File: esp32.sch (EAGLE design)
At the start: 2 parts, among them IC1 PEC11R-4230K-S0024, U1 ESP32-WROOM-32D

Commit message: Stora dela av schematic är klart. Saknar fortfarande vissa viktiga delar, men då måste jag passera admittansen först.
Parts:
- added 5V_REG_CON, WS2812B_CON: (no value), SparkFun-Connectors:CONN_03
- added BAT_CON, SPEAKER_OUT: (no value), SparkFun-Connectors:CONN_02
- added C1, C2, C3, C4, C5, C6: (no value), rcl:C-EUC0603
- added C7, C8: 10uF, rcl:C-EUC0603
- added C9: 270uF, rcl:C-EUC0603
- added DS1: (no value), Test:NHD-0216XZ-FSW-GBWNHD0216XZFSWGBW_DUPONTCONNECTOR
- added IC2: AD8532ARZ, Test:AD8532ARZ
- added JP1, JP2: (no value), pinhead:PINHD-1X2
- added R1, R10, R12, R14, R2, R3, R4, R5, R6, R8: 10k, rcl:R-EU_R0603
- added R11, R13, R22, R7, R9: 100, rcl:R-EU_R0603
- added R15, R16: (no value), rcl:R-EU_R0603
- added R17, R18, R21: 50k, rcl:R-EU_R0603
- added R19: 100k, rcl:R-EU_R0603
- added R20: 16, rcl:R-EU_R0603
- added T1, T2: BST82-1, Test:BST82-1
- added U$1, U$2, U$3: PUSH_BUTTON, Test:PUSH_BUTTON
- added U$4: A1SHB, Test:A1SHB
- added U$5: ESP32_CON_JTAG, Test:ESP32_CON_JTAG
- added U$6: ESP32_CON_PROG, Test:ESP32_CON_PROG
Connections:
- new net +3V3: IC1.COM, R3.1, R4.1, U$1.1, U$1.2, U$2.1, U$2.2, U$3.1, U$3.2
- new net +5V: 5V_REG_CON.2, WS2812B_CON.1
- new net AUDIO_FROM_ESP32: C8.1
- new net BAT_MONITOR_ANALOG: R15.2, R16.1
- new net BAT_MONITOR_ENABLE: R13.2
- new net BTN_1: R7.1
- new net BTN_2: R9.1
- new net BTN_3: R11.1
- new net ENABLE_5V: R22.2
- new net ESP_EN: U$6.EN
- new net ESP_IO_0: U$6.IO_0
- new net ESP_RX: U$6.ESP_RX
- new net ESP_TX: U$6.ESP_TX
- new net GND: BAT_CON.2, C1.2, C2.2, C3.2, C4.2, C5.2, C6.2, IC1.C, IC2.V-, R10.1, R12.1, R16.2, R19.1, R21.2, R6.1, R8.1, SPEAKER_OUT.2, T1.S, T2.S, U$5.GND, U$6.GND, WS2812B_CON.3
- new net N$1: IC1.A, R1.2, R3.2
- new net N$10: C7.1, R17.1, R18.2
- new net N$11: R22.1, T2.G
- new net N$12: IC2.-INA, IC2.OUTA, R20.2
- new net N$13: R13.1, T1.G
- new net N$14: C9.1, R20.1
- new net N$15: 5V_REG_CON.3, T2.D
- new net N$2: IC1.B, R2.1, R4.2
- new net N$22: JP2.2, U$6.VDD
- new net N$23: JP2.1
- new net N$24: JP1.1, U$5.VDD
- new net N$25: JP1.2
- new net N$3: C4.1, R7.2, R8.2, U$1.3, U$1.4
- new net N$4: C8.2, IC2.+INA, R18.1, R19.2
- new net N$5: R15.1, U$4.D
- new net N$6: C5.1, R10.2, R9.2, U$2.3, U$2.4
- new net N$7: R14.2, T1.D, U$4.G
- new net N$8: C6.1, R11.2, R12.2, U$3.3, U$3.4
- new net N$9: C3.1, IC1.NO, R5.2, R6.2
- new net ROT_ENC_A: C1.1, R1.1
- new net ROT_ENC_B: C2.1, R2.2
- new net ROT_ENC_BTN: R5.1
- new net SPEAKER_OUT: C9.2, R21.1, SPEAKER_OUT.1
- new net TCK: U$5.TCK
- new net TDI: U$5.TDI
- new net TDO: U$5.TDO
- new net TMS: U$5.TMS
- new net VCC: 5V_REG_CON.1, BAT_CON.1, IC2.V+, R14.1, R17.2, U$4.S
- new net WS2812B_DATA: WS2812B_CON.2
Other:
- note added: "3.3V regulator här sen tack"

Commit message: Lite grovt upplägg av vissa komponenter på kortet.
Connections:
- net +3V3: now also U1.3V3
- net AUDIO_FROM_ESP32: now also U1.IO26
- net ESP_EN: now also U1.EN
- net ESP_IO_0: now also U1.IO25
- net ESP_RX: now also U1.RXD0
- net ESP_TX: now also U1.TXD0
- net GND: now also C7.2, U1.GND
- net TCK: now also U1.IO13
- net TDI: now also U1.IO12
- net TDO: now also U1.IO15
- net TMS: now also U1.IO14
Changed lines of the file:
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@@
 <part name="GND17" library="supply1" library_urn="urn:adsk.eagle:library:371" deviceset="GND" device=""/>
 <part name="GND18" library="supply1" library_urn="urn:adsk.eagle:library:371" deviceset="GND" device=""/>
+<part name="GND19" library="supply1" library_urn="urn:adsk.eagle:library:371" deviceset="GND" device=""/>
+<part name="GND20" library="supply1" library_urn="urn:adsk.eagle:library:371" deviceset="GND" device=""/>
+<part name="+3V6" library="supply1" library_urn="urn:adsk.eagle:library:371" deviceset="+3V3" device=""/>
 </parts>
 <sheets>
@@
 <attribute name="VALUE" x="121.92" y="119.38" size="1.778" layer="96"/>
 </instance>
+<instance part="GND20" gate="1" x="83.82" y="81.28" smashed="yes">
+<attribute name="VALUE" x="81.28" y="78.74" size="1.778" layer="96"/>
+</instance>
+<instance part="+3V6" gate="G$1" x="83.82" y="160.02" smashed="yes">
+<attribute name="VALUE" x="81.28" y="154.94" size="1.778" layer="96" rot="R90"/>
+</instance>
 </instances>
 <busses>
@@
 <wire x1="167.64" y1="93.98" x2="167.64" y2="76.2" width="0.1524" layer="91"/>
 </segment>
+<segment>
+<pinref part="U1" gate="G$1" pin="GND"/>
+<wire x1="81.28" y1="91.44" x2="83.82" y2="91.44" width="0.1524" layer="91"/>
+<wire x1="83.82" y1="91.44" x2="83.82" y2="83.82" width="0.1524" layer="91"/>
+<pinref part="GND20" gate="1" pin="GND"/>
+</segment>
 </net>
 <net name="+5V" class="0">
@@
 <label x="165.1" y="142.24" size="1.778" layer="95" xref="yes"/>
 </segment>
+<segment>
+<pinref part="U1" gate="G$1" pin="IO14"/>
+<wire x1="81.28" y1="129.54" x2="93.98" y2="129.54" width="0.1524" layer="91"/>
+<label x="93.98" y="129.54" size="1.778" layer="95" xref="yes"/>
+</segment>
 </net>
 <net name="TCK" class="0">
@@
 <label x="165.1" y="137.16" size="1.778" layer="95" xref="yes"/>
 </segment>
+<segment>
+<pinref part="U1" gate="G$1" pin="IO13"/>
+<wire x1="81.28" y1="132.08" x2="86.36" y2="132.08" width="0.1524" layer="91"/>
+<label x="86.36" y="132.08" size="1.778" layer="95" xref="yes"/>
+</segment>
 </net>
 <net name="TDO" class="0">
@@
 <wire x1="160.02" y1="132.08" x2="165.1" y2="132.08" width="0.1524" layer="91"/>
 <label x="165.1" y="132.08" size="1.778" layer="95" xref="yes"/>
+</segment>
+<segment>
+<pinref part="U1" gate="G$1" pin="IO15"/>
+<wire x1="81.28" y1="127" x2="86.36" y2="127" width="0.1524" layer="91"/>
+<label x="86.36" y="127" size="1.778" layer="95" xref="yes"/>
 </segment>
 </net>
@@
 <label x="165.1" y="127" size="1.778" layer="95" xref="yes"/>
 </segment>
+<segment>
+<pinref part="U1" gate="G$1" pin="IO12"/>
+<wire x1="81.28" y1="134.62" x2="93.98" y2="134.62" width="0.1524" layer="91"/>
+<label x="93.98" y="134.62" size="1.778" layer="95" xref="yes"/>
+</segment>
 </net>
 <net name="N$22" class="0">
@@
 <wire x1="132.08" y1="99.06" x2="132.08" y2="96.52" width="0.1524" layer="91"/>
 </segment>
+<segment>
+<pinref part="U1" gate="G$1" pin="EN"/>
+<wire x1="40.64" y1="144.78" x2="38.1" y2="144.78" width="0.1524" layer="91"/>
+<label x="38.1" y="144.78" size="1.778" layer="95" rot="R180" xref="yes"/>
+</segment>
 </net>
 <net name="ESP_TX" class="0">
@@
 <wire x1="134.62" y1="93.98" x2="132.08" y2="93.98" width="0.1524" layer="91"/>
 <label x="132.08" y="93.98" size="1.778" layer="95" rot="R180" xref="yes"/>
+</segment>
+<segment>
+<pinref part="U1" gate="G$1" pin="TXD0"/>
+<wire x1="40.64" y1="121.92" x2="38.1" y2="121.92" width="0.1524" layer="91"/>
+<label x="38.1" y="124.46" size="1.778" layer="95" rot="R180" xref="yes"/>
+<wire x1="38.1" y1="121.92" x2="38.1" y2="124.46" width="0.1524" layer="91"/>
 </segment>
 </net>
@@
 <wire x1="132.08" y1="91.44" x2="132.08" y2="88.9" width="0.1524" layer="91"/>
 </segment>
+<segment>
+<pinref part="U1" gate="G$1" pin="RXD0"/>
+<wire x1="40.64" y1="119.38" x2="38.1" y2="119.38" width="0.1524" layer="91"/>
+<label x="38.1" y="116.84" size="1.778" layer="95" rot="R180" xref="yes"/>
+<wire x1="38.1" y1="119.38" x2="38.1" y2="116.84" width="0.1524" layer="91"/>
+</segment>
 </net>
 <net name="ESP_IO_0" class="0">
@@
 <wire x1="165.1" y1="91.44" x2="170.18" y2="91.44" width="0.1524" layer="91"/>
 <label x="170.18" y="91.44" size="1.778" layer="95" xref="yes"/>
+</segment>
+<segment>
+<pinref part="U1" gate="G$1" pin="IO25"/>
+<wire x1="81.28" y1="106.68" x2="88.9" y2="106.68" width="0.1524" layer="91"/>
+<label x="88.9" y="106.68" size="1.778" layer="95" xref="yes"/>
+</segment>
+</net>
+<net name="+3V3" class="0">
+<segment>
+<pinref part="U1" gate="G$1" pin="3V3"/>
+<wire x1="81.28" y1="149.86" x2="83.82" y2="149.86" width="0.1524" layer="91"/>
+<wire x1="83.82" y1="149.86" x2="83.82" y2="157.48" width="0.1524" layer="91"/>
+<pinref part="+3V6" gate="G$1" pin="+3V3"/>
+</segment>
+</net>
+<net name="AUDIO_FROM_ESP32" class="0">
+<segment>
+<pinref part="U1" gate="G$1" pin="IO26"/>
+<wire x1="81.28" y1="104.14" x2="83.82" y2="104.14" width="0.1524" layer="91"/>
+<label x="83.82" y="104.14" size="1.778" layer="95" xref="yes"/>
 </segment>
 </net>
@@
 </instance>
 <instance part="R8" gate="G$1" x="185.42" y="144.78" smashed="yes" rot="R90">
-<attribute name="NAME" x="183.9214" y="140.97" size="1.778" layer="95" rot="R90"/>
-<attribute name="VALUE" x="188.722" y="140.97" size="1.778" layer="96" rot="R90"/>
+<attribute name="NAME" x="178.8414" y="140.97" size="1.778" layer="95" rot="R90"/>
+<attribute name="VALUE" x="183.642" y="140.97" size="1.778" layer="96" rot="R90"/>
 </instance>
 <instance part="C4" gate="G$1" x="193.04" y="147.32" smashed="yes">
@@
 <attribute name="VALUE" x="137.16" y="48.26" size="1.778" layer="96"/>
 </instance>
+<instance part="GND19" gate="1" x="66.04" y="45.72" smashed="yes">
+<attribute name="VALUE" x="63.5" y="43.18" size="1.778" layer="96"/>
+</instance>
 </instances>
 <busses>
@@
 <wire x1="139.7" y1="53.34" x2="139.7" y2="60.96" width="0.1524" layer="91"/>
 </segment>
-</net>
+<segment>
+<pinref part="GND19" gate="1" pin="GND"/>
+<pinref part="C7" gate="G$1" pin="2"/>
+<wire x1="66.04" y1="48.26" x2="66.04" y2="50.8" width="0.1524" layer="91"/>
+</segment>
+</net>

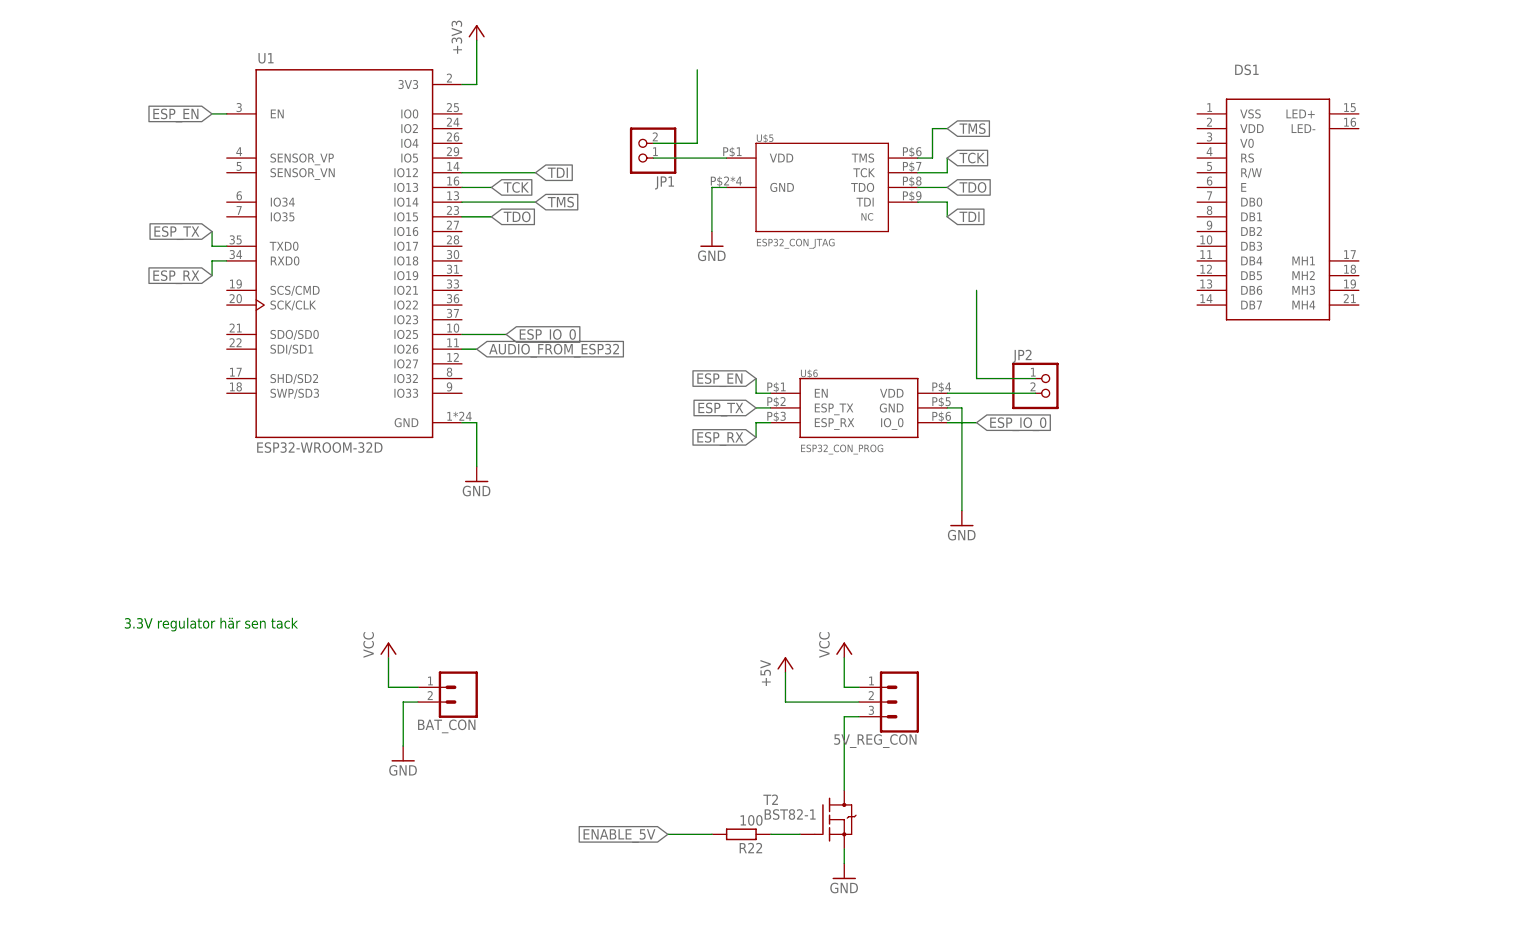
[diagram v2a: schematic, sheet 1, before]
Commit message: Bra upplägg på kortet men saknar fortfarande 3.3V regulator.
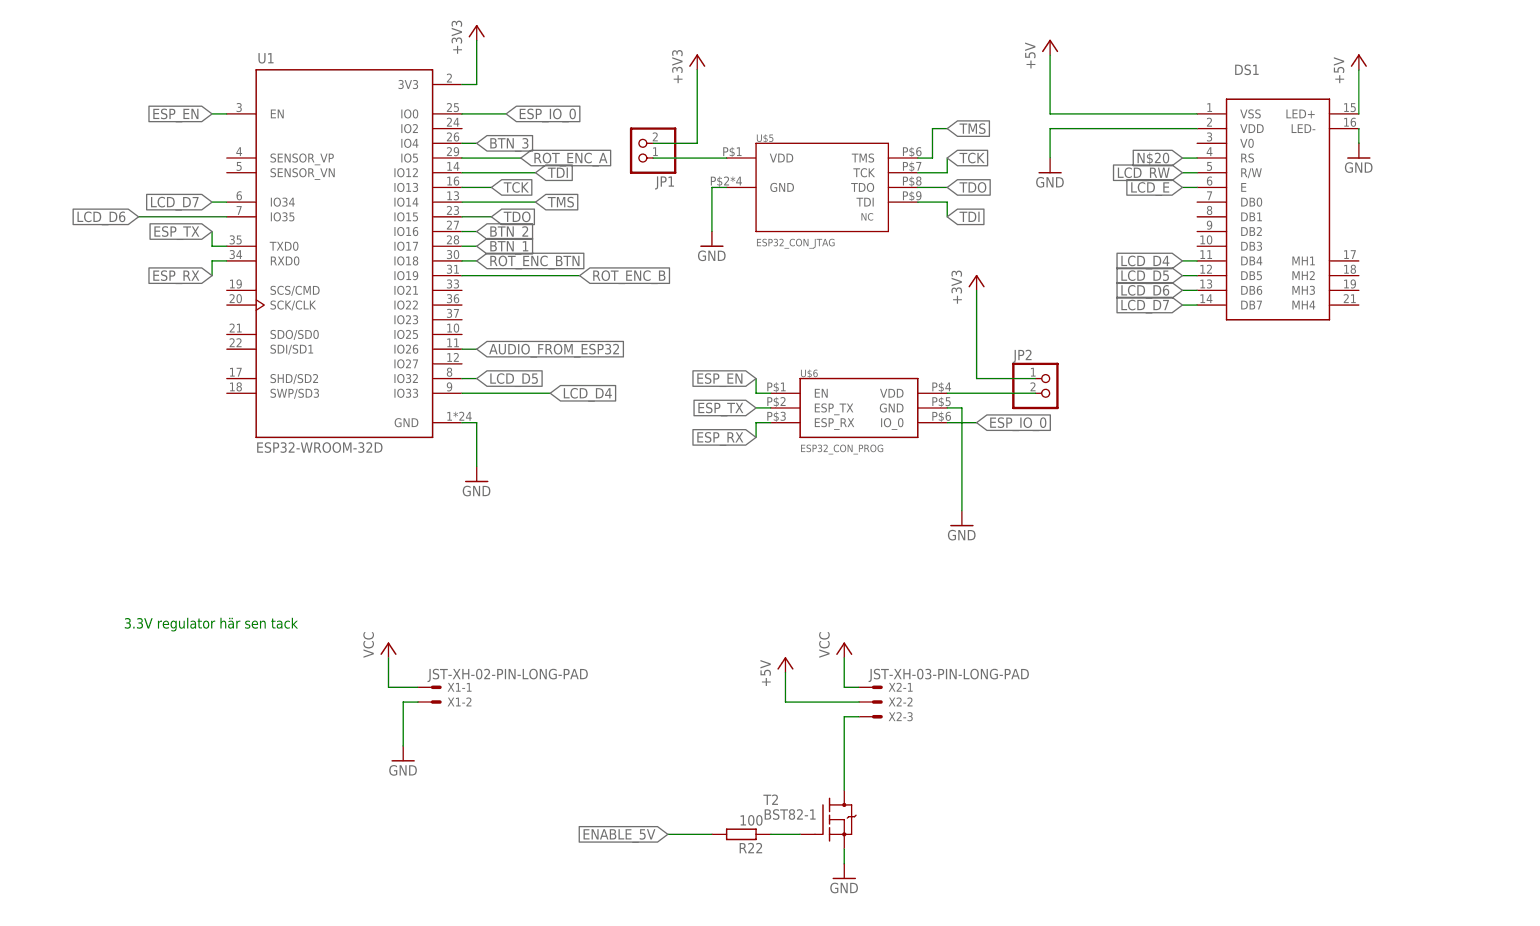
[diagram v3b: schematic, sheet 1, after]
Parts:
- removed 5V_REG_CON, WS2812B_CON: (no value), SparkFun-Connectors:CONN_03
- removed BAT_CON, SPEAKER_OUT: (no value), SparkFun-Connectors:CONN_02
- added X1, X4: JST-XH-02-PIN-LONG-PAD, Rembrandt Electronics - JST XH Connectors v1-0:JST-XH-02-PIN-LONG-PAD
- added X2, X3: JST-XH-03-PIN-LONG-PAD, Rembrandt Electronics - JST XH Connectors v1-0:JST-XH-03-PIN-LONG-PAD
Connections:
- removed net N$23: JP2.1
- removed net N$25: JP1.2
- new net LCD_D4: DS1.DB4, U1.IO33
- new net LCD_D5: DS1.DB5, U1.IO32
- new net LCD_D6: DS1.DB6, U1.IO35
- new net LCD_D7: DS1.DB7, U1.IO34
- new net LCD_E: DS1.E
- new net LCD_RW: DS1.R/W
- new net N$20: DS1.RS
- net +3V3: now also JP1.2, JP2.1
- net +5V: now also DS1.LED+, DS1.VSS, X2-2.S, X3-1.S; no longer 5V_REG_CON.2, WS2812B_CON.1
- net BTN_1: now also U1.IO17
- net BTN_2: now also U1.IO16
- net BTN_3: now also U1.IO4
- net ESP_IO_0: now also U1.IO0; no longer U1.IO25
- net GND: now also DS1.LED-, DS1.VDD, X1-2.S, X3-3.S, X4-2.S; no longer BAT_CON.2, SPEAKER_OUT.2, WS2812B_CON.3
- net N$15: now also X2-3.S; no longer 5V_REG_CON.3
- net ROT_ENC_A: now also U1.IO5
- net ROT_ENC_B: now also U1.IO19
- net ROT_ENC_BTN: now also U1.IO18
- net SPEAKER_OUT: now also X4-1.S; no longer SPEAKER_OUT.1
- net VCC: now also X1-1.S, X2-1.S; no longer 5V_REG_CON.1, BAT_CON.1
- net WS2812B_DATA: now also X3-2.S; no longer WS2812B_CON.2

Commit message: Kom på att man ska lägga till en reset-knapp... Men saknar fortfarande massa kondingar och sen 3.3V regulator.
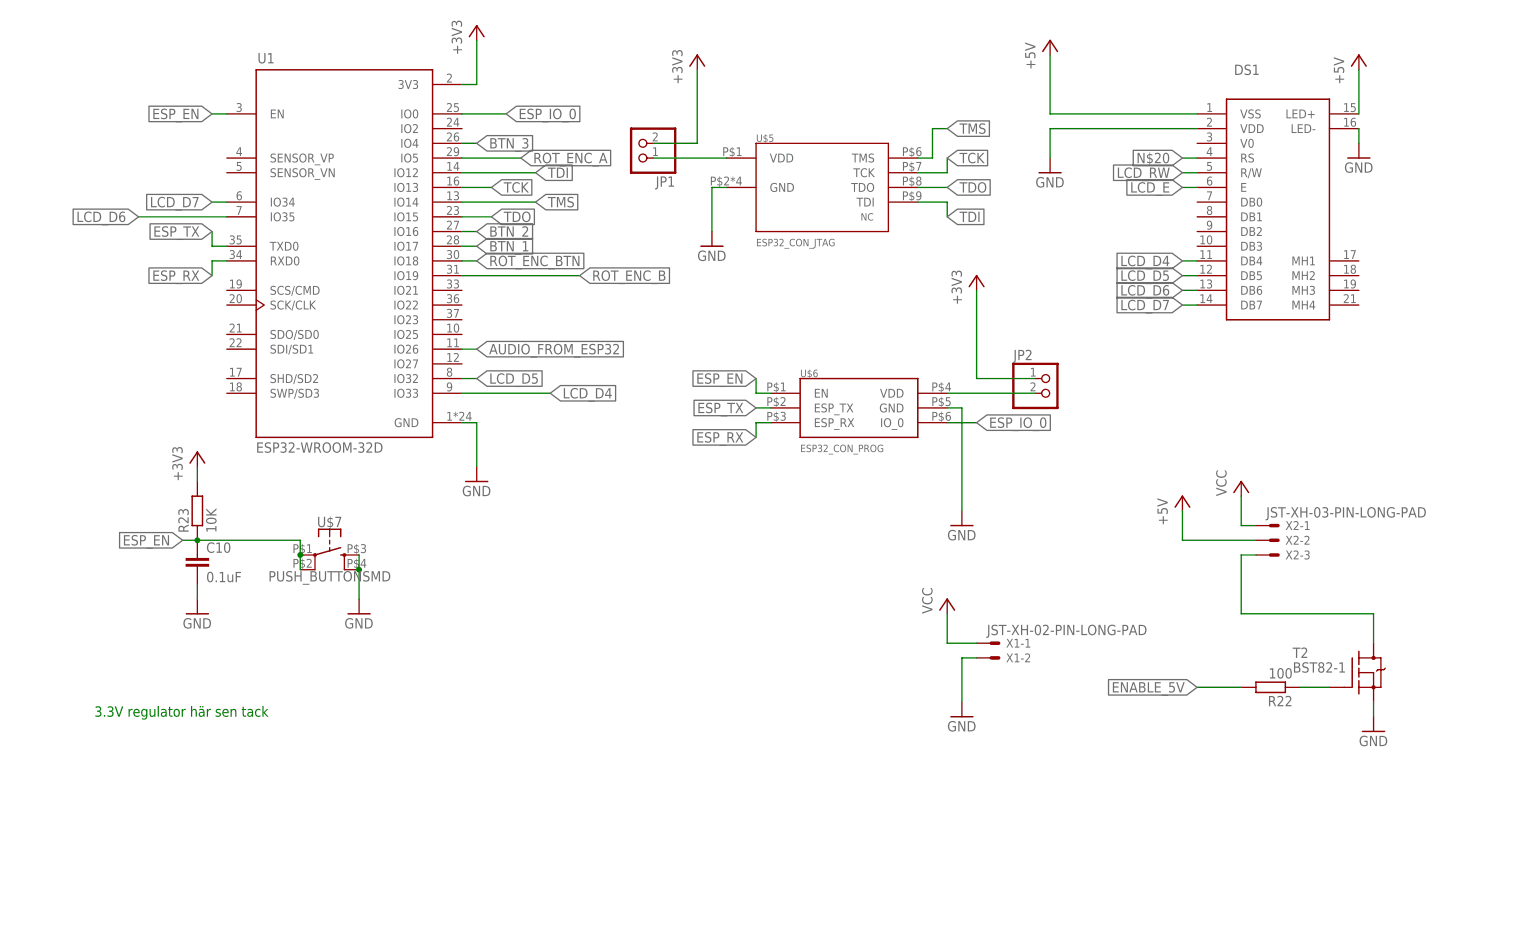
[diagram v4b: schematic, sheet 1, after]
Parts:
- added C10: 0.1uF, rcl:C-EUC0603
- added R23: 10K, rcl:R-EU_R0603
- added U$7: PUSH_BUTTONSMD, Test:PUSH_BUTTONSMD
- IC1: value PEC11R-4230K-S0024 -> PEC11R-4230K-S00243D; device Test:PEC11R-4230K-S0024 -> Test:PEC11R-4230K-S00243D
- U$1, U$2, U$3: value PUSH_BUTTON -> PUSH_BUTTONSMD; device Test:PUSH_BUTTON -> Test:PUSH_BUTTONSMD
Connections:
- net +3V3: now also R23.2
- net ESP_EN: now also C10.1, R23.1, U$7.1, U$7.2
- net GND: now also C10.2, U$7.3, U$7.4
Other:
- moved on the sheet: R22, T2, X1-1, X1-2, X2-1, X2-2, X2-3
